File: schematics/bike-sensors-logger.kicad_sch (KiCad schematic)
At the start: 2 parts, among them U1 RaspberryPi_Zero_Dummy

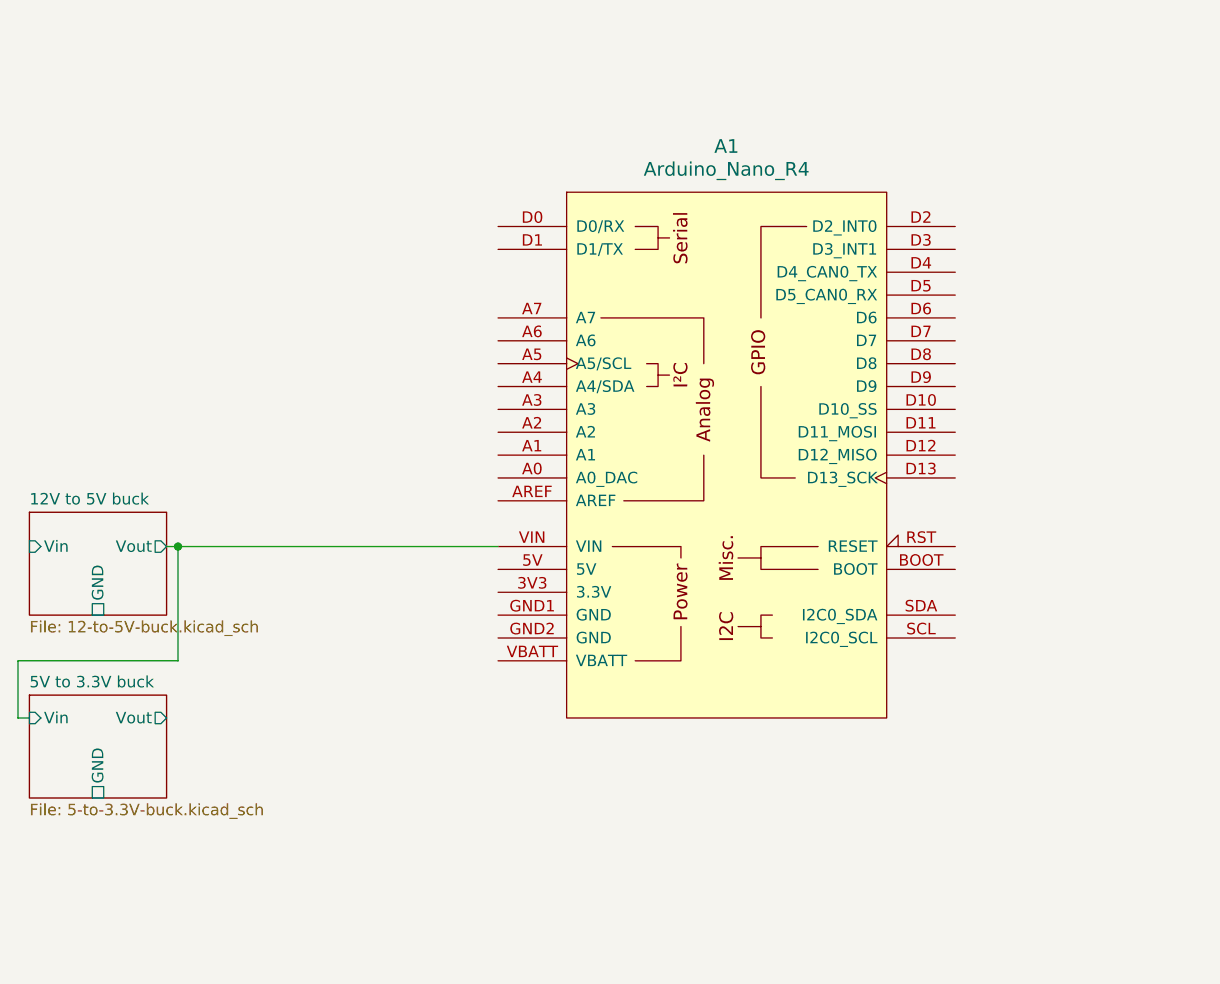
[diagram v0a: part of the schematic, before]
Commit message: Added accelerometer + gyroscope
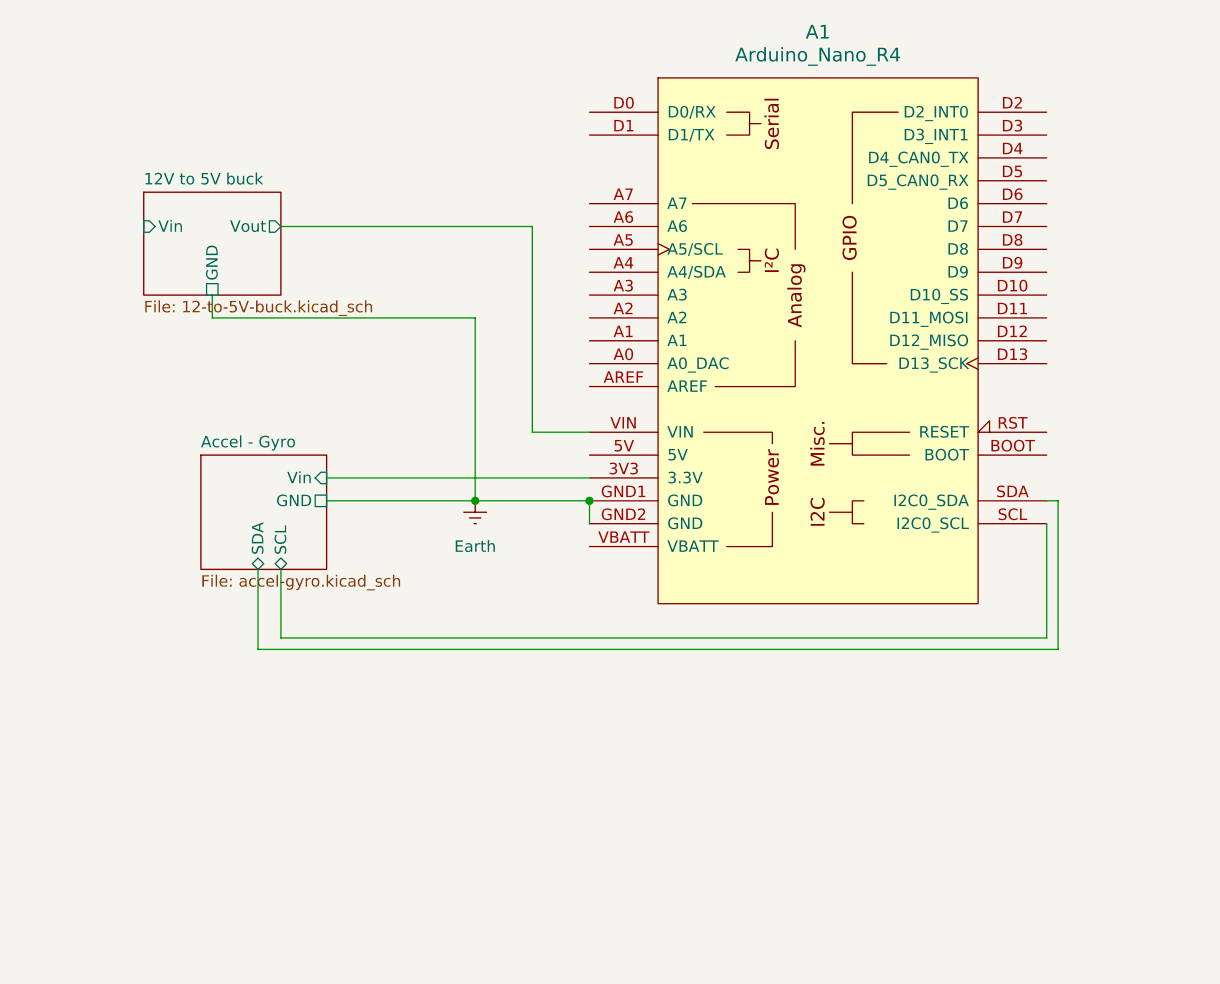
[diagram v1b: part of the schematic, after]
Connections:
- net Accel - Gyro/Vin: now reaches A1.3V3 (3.3V)
- net Earth: now reaches A1.GND1 (GND)
- net Earth: now also A1.GND2 (GND)
- net Accel - Gyro/SCL: now reaches A1.SCL (I2C0_SCL)
- net Accel - Gyro/SDA: now reaches A1.SDA (I2C0_SDA)
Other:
- removed sheet 5V to 3.3V buck
- added sheet Accel - Gyro (accel-gyro.kicad_sch)
- moved on the sheet: A1

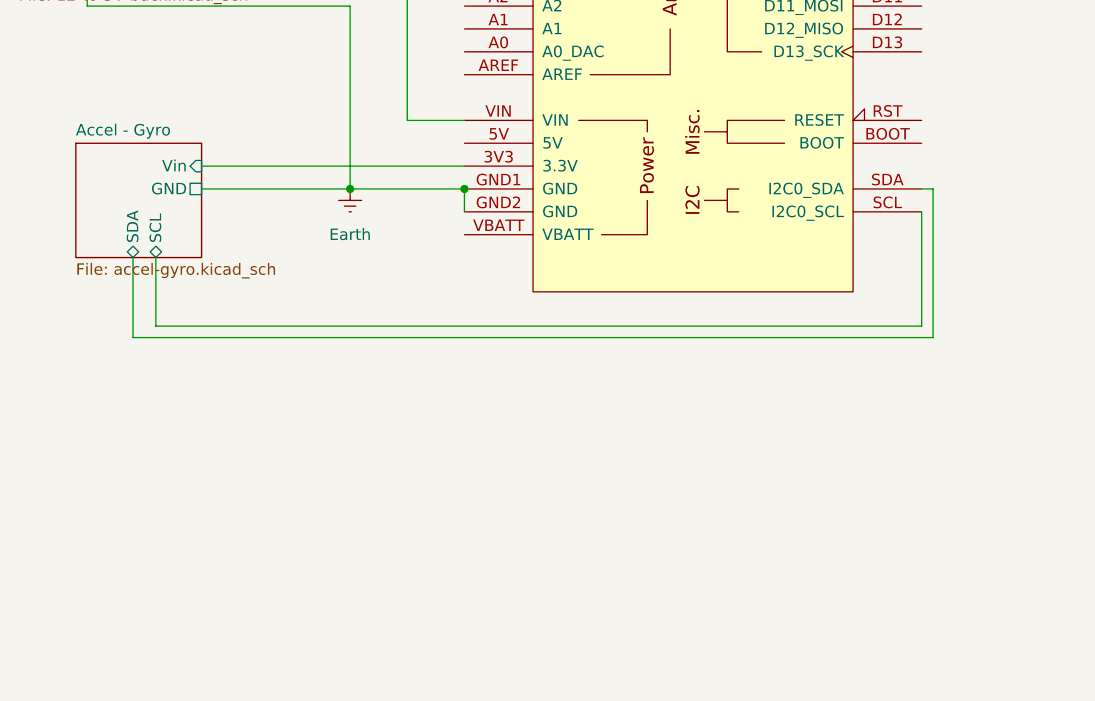
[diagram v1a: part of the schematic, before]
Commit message: Added GNSS module
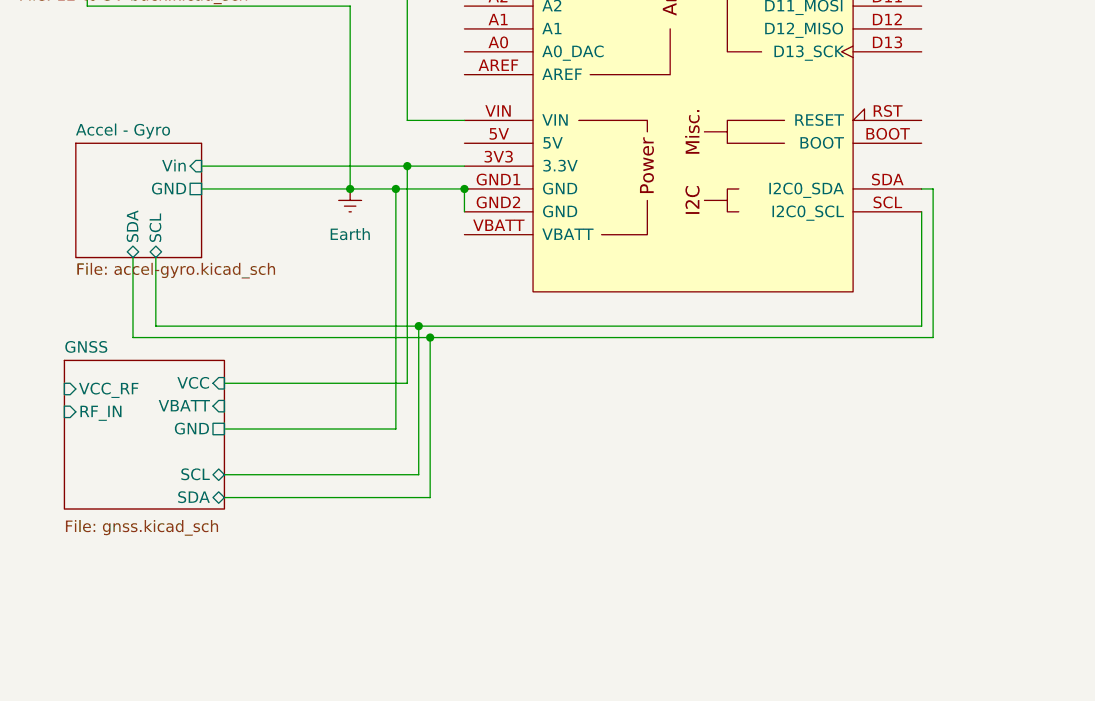
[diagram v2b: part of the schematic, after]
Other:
- added sheet GNSS (gnss.kicad_sch)
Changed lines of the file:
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@@
+	)
+	(junction
+		(at 82.55 87.63)
+		(diameter 0)
+		(color 0 0 0 0)
+	)
+	(junction
+		(at 81.28 69.85)
+		(diameter 0)
+		(color 0 0 0 0)
+	)
+	(junction
+		(at 80.01 72.39)
+		(diameter 0)
+		(color 0 0 0 0)
 	)
 	(junction
@@
 		(color 0 0 0 0)
 	)
+	(junction
+		(at 83.82 88.9)
+		(diameter 0)
+		(color 0 0 0 0)
+	)
+	(wire
+		(pts
+			(xy 82.55 104.14) (xy 82.55 87.63)
+		)
+		(stroke
+			(width 0)
+			(type default)
+		)
+	)
 	(wire
 		(pts
@@
 	(wire
 		(pts
-			(xy 74.93 72.39) (xy 87.63 72.39)
+			(xy 74.93 72.39) (xy 80.01 72.39)
+		)
+		(stroke
+			(width 0)
+			(type default)
+		)
+	)
+	(wire
+		(pts
+			(xy 60.96 99.06) (xy 80.01 99.06)
+		)
+		(stroke
+			(width 0)
+			(type default)
+		)
+	)
+	(wire
+		(pts
+			(xy 81.28 93.98) (xy 81.28 69.85)
 		)
 		(stroke
@@
 	(wire
 		(pts
-			(xy 53.34 87.63) (xy 138.43 87.63)
+			(xy 83.82 88.9) (xy 139.7 88.9)
+		)
+		(stroke
+			(width 0)
+			(type default)
+		)
+	)
+	(wire
+		(pts
+			(xy 53.34 87.63) (xy 82.55 87.63)
 		)
 		(stroke
@@
 	(wire
 		(pts
+			(xy 83.82 106.68) (xy 83.82 88.9)
+		)
+		(stroke
+			(width 0)
+			(type default)
+		)
+	)
+	(wire
+		(pts
+			(xy 82.55 87.63) (xy 138.43 87.63)
+		)
+		(stroke
+			(width 0)
+			(type default)
+		)
+	)
+	(wire
+		(pts
 			(xy 58.42 72.39) (xy 74.93 72.39)
 		)
@@
 	(wire
 		(pts
+			(xy 60.96 106.68) (xy 83.82 106.68)
+		)
+		(stroke
+			(width 0)
+			(type default)
+		)
+	)
+	(wire
+		(pts
 			(xy 74.93 52.07) (xy 74.93 72.39)
 		)
@@
 	(wire
 		(pts
+			(xy 80.01 99.06) (xy 80.01 72.39)
+		)
+		(stroke
+			(width 0)
+			(type default)
+		)
+	)
+	(wire
+		(pts
+			(xy 60.96 104.14) (xy 82.55 104.14)
+		)
+		(stroke
+			(width 0)
+			(type default)
+		)
+	)
+	(wire
+		(pts
+			(xy 80.01 72.39) (xy 87.63 72.39)
+		)
+		(stroke
+			(width 0)
+			(type default)
+		)
+	)
+	(wire
+		(pts
 			(xy 138.43 72.39) (xy 139.7 72.39)
 		)
@@
 	(wire
 		(pts
-			(xy 58.42 69.85) (xy 87.63 69.85)
-		)
-		(stroke
-			(width 0)
-			(type default)
-		)
-	)
-	(wire
-		(pts
-			(xy 50.8 88.9) (xy 139.7 88.9)
+			(xy 81.28 69.85) (xy 87.63 69.85)
+		)
+		(stroke
+			(width 0)
+			(type default)
+		)
+	)
+	(wire
+		(pts
+			(xy 58.42 69.85) (xy 81.28 69.85)
+		)
+		(stroke
+			(width 0)
+			(type default)
+		)
+	)
+	(wire
+		(pts
+			(xy 50.8 88.9) (xy 83.82 88.9)
 		)
 		(stroke
@@
 		(pts
 			(xy 87.63 72.39) (xy 87.63 74.93)
+		)
+		(stroke
+			(width 0)
+			(type default)
+		)
+	)
+	(wire
+		(pts
+			(xy 60.96 93.98) (xy 81.28 93.98)
 		)
 		(stroke
@@
 				)
 			)
+		)
+	)
+	(sheet
+		(at 43.18 91.44)
+		(size 17.78 16.51)
+		(exclude_from_sim no)
+		(in_bom yes)
+		(on_board yes)
+		(dnp no)
+		(fields_autoplaced yes)
+		(stroke
+			(width 0.1524)
+			(type solid)
+		)
+		(fill
+			(color 0 0 0 0.0000)
+		)
+		(property "Sheetname" "GNSS"
+			(at 43.18 90.7284 0)
+			(effects
+				(font
+					(size 1.27 1.27)
+				)
+				(justify left bottom)
+			)
+		)
+		(property "Sheetfile" "gnss.kicad_sch"
+			(at 43.18 109.1696 0)
+			(effects
+				(font
+					(size 1.27 1.27)
+				)
+				(justify left top)
+			)
+		)
+		(pin "GND" passive
+			(at 60.96 99.06 0)
+			(effects
+				(font
+					(size 1.27 1.27)
+				)
+				(justify right)
+			)
+		)
+		(pin "RF_IN" input
+			(at 43.18 97.155 180)
+			(effects
+				(font
+					(size 1.27 1.27)
+				)
+				(justify left)
+			)
+		)
+		(pin "SCL" bidirectional
+			(at 60.96 104.14 0)
+			(effects
+				(font
+					(size 1.27 1.27)
+				)
+				(justify right)
+			)
+		)
+		(pin "SDA" bidirectional
+			(at 60.96 106.68 0)
+			(effects
+				(font
+					(size 1.27 1.27)
+				)
+				(justify right)
+			)
+		)
+		(pin "VBATT" input
+			(at 60.96 96.52 0)
+			(effects
+				(font
+					(size 1.27 1.27)
+				)
+				(justify right)
+			)
+		)
+		(pin "VCC" input
+			(at 60.96 93.98 0)
+			(effects
+				(font
+					(size 1.27 1.27)
+				)
+				(justify right)
+			)
+		)
+		(pin "VCC_RF" input
+			(at 43.18 94.615 180)
+			(effects
+				(font
+					(size 1.27 1.27)
+				)
+				(justify left)
+			)
+		)
+		(instances
+			(project "bike-sensors-logger"
+				(path "/2c1d9222-af16-428b-85a5-a3d420373d70"
+					(page "4")
+				)
+			)

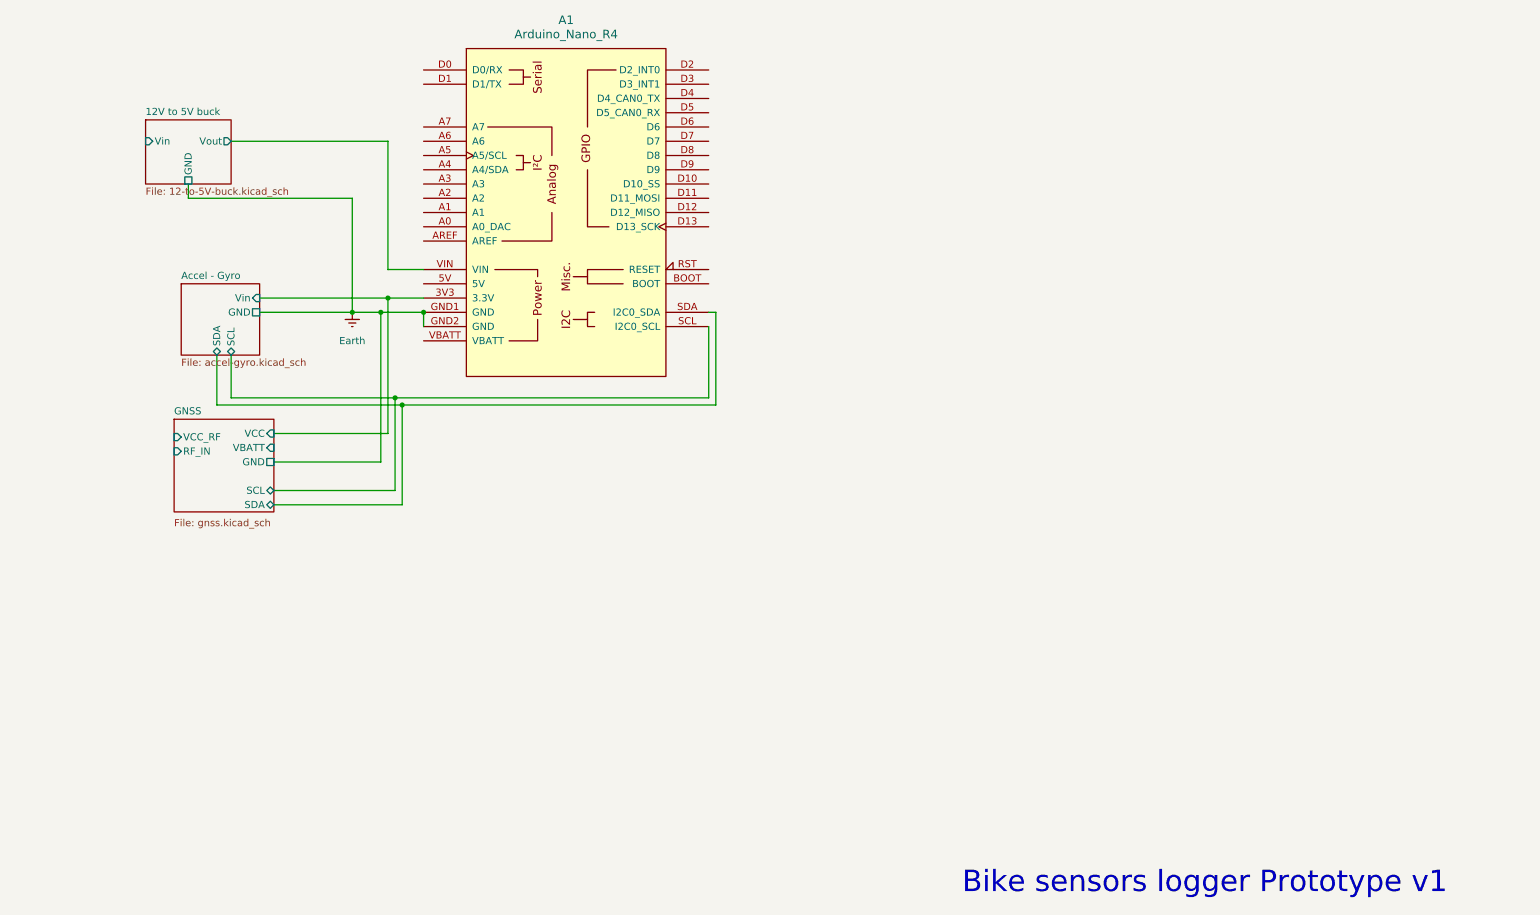
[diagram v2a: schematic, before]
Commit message: Normalized sheet titles; added MMCX connector for GPS antenna + active antenna power switch
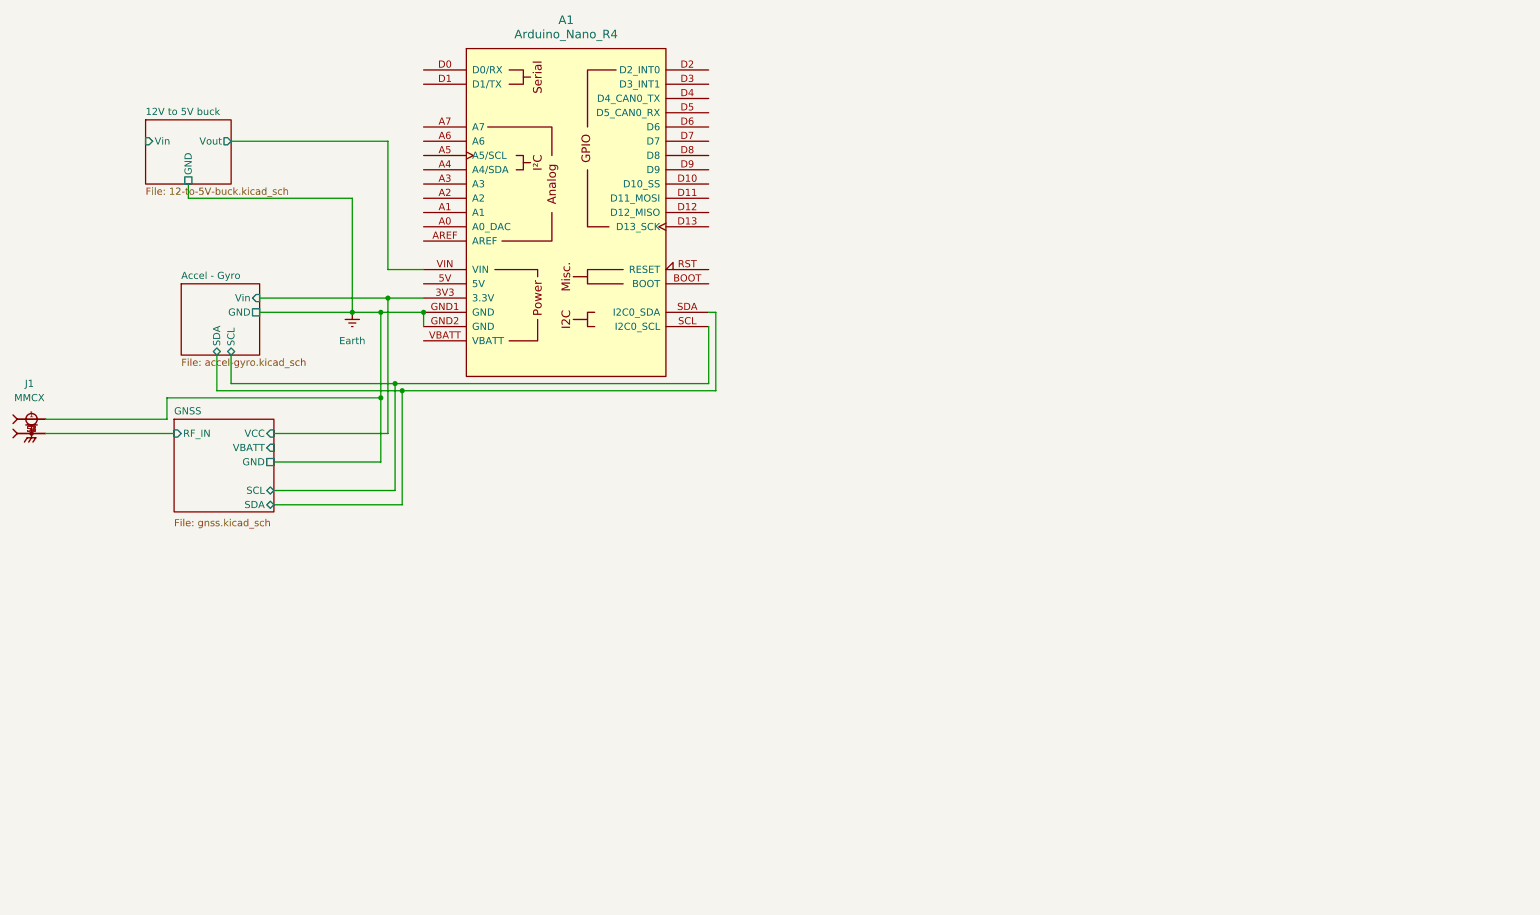
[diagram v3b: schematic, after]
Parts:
- added J1: MMCX, 0732511352:MOLEX_0732511352, symbol 0732511352:0732511352
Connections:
- net Earth: now also J1.1
- net GNSS/RF_IN: now also J1.S1, J1.S2, J1.S3, J1.S4
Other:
- sheet GNSS ports: added none; removed VCC_RF
- note removed: "Bike sensors logger Prototype v1"
- title: (none) -> Bike sensors logger MK1

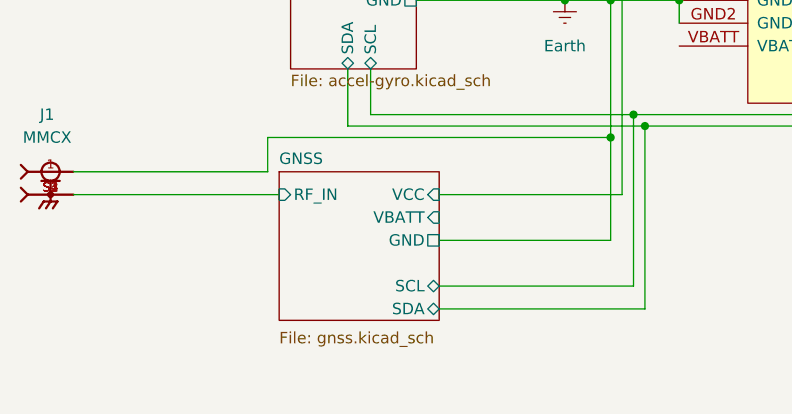
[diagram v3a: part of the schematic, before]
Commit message: Added ANT_PWR pin to signal the GNSS switch's state (TODO: link to a status LED)
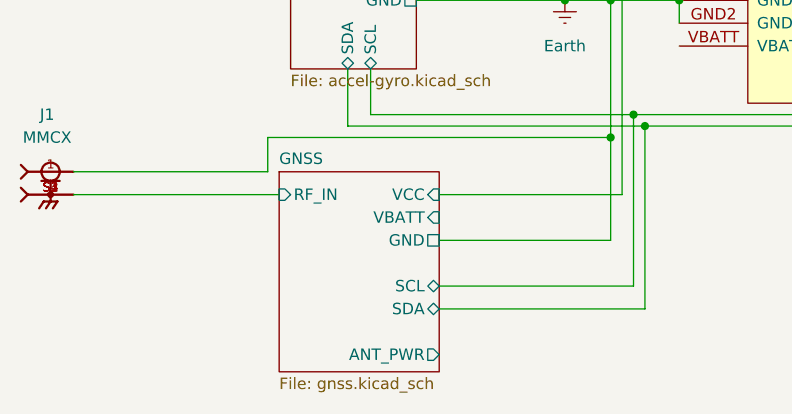
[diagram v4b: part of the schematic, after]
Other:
- sheet GNSS ports: added ANT_PWR; removed none
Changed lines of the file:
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@@
 	(sheet
 		(at 43.18 91.44)
-		(size 17.78 16.51)
+		(size 17.78 22.225)
 		(exclude_from_sim no)
 		(in_bom yes)
@@
 		)
 		(property "Sheetfile" "gnss.kicad_sch"
-			(at 43.18 109.1696 0)
+			(at 43.18 114.2496 0)
 			(effects
 				(font
@@
 			(effects
 				(font
+					(size 1.27 1.27)
+				)
+				(justify right)
+			)
+		)
+		(pin "ANT_PWR" output
+			(at 60.96 111.76 0)
+			(effects
+				(font
